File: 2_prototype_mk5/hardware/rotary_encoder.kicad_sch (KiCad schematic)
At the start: 2 parts, among them J8 Conn_01x05, SW2 PEC12R-2120F-S0012

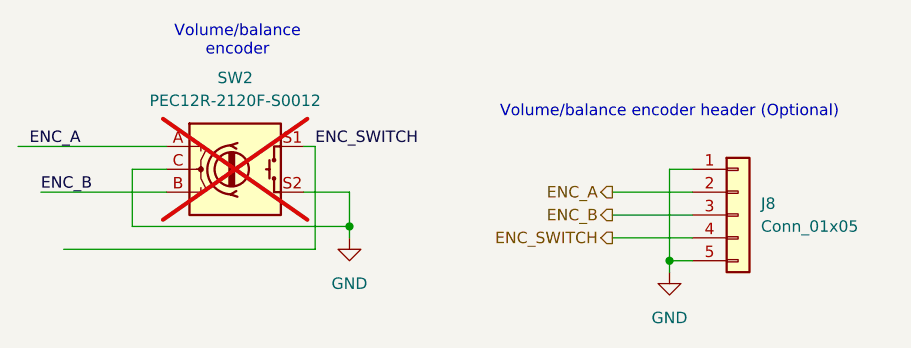
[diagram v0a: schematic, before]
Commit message: Major MKV redesign using embedded RP2350
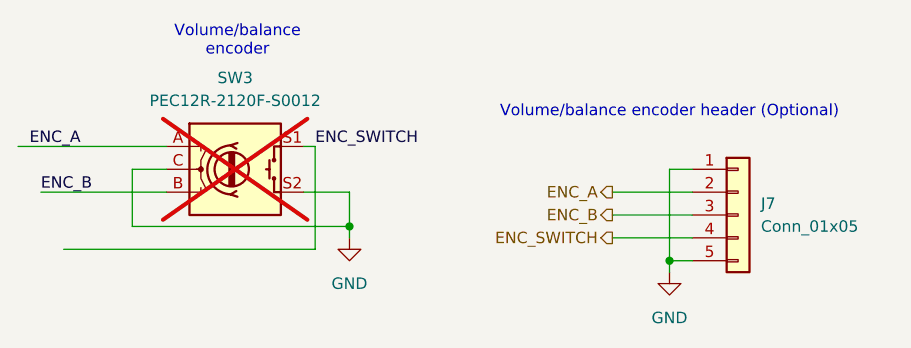
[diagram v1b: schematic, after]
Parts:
- renumbered J8 to J7, SW2 to SW3
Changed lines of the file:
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@@
 		(dnp no)
 		(fields_autoplaced yes)
-		(property "Reference" "#PWR031"
+		(property "Reference" "#PWR049"
 			(at 158.75 91.44 0)
 			(hide yes)
@@
 			(project "HDD Synth Prototype MK5"
 				(path "/1a22431a-ba36-40a0-9a7e-c2a82ec69c53/293c32c0-b0ed-4b60-a32a-d04548ae7be6"
-					(reference "#PWR031")
+					(reference "#PWR049")
 					(unit 1)
 				)
@@
 		(dnp yes)
 		(fields_autoplaced yes)
-		(property "Reference" "SW2"
+		(property "Reference" "SW3"
 			(at 146.05 67.31 0)
 			(show_name no)
@@
 			(project "HDD Synth Prototype MK5"
 				(path "/1a22431a-ba36-40a0-9a7e-c2a82ec69c53/293c32c0-b0ed-4b60-a32a-d04548ae7be6"
-					(reference "SW2")
+					(reference "SW3")
 					(unit 1)
 				)
@@
 		(dnp no)
 		(fields_autoplaced yes)
-		(property "Reference" "#PWR032"
+		(property "Reference" "#PWR050"
 			(at 194.31 95.25 0)
 			(hide yes)
@@
 			(project "HDD Synth Prototype MK5"
 				(path "/1a22431a-ba36-40a0-9a7e-c2a82ec69c53/293c32c0-b0ed-4b60-a32a-d04548ae7be6"
-					(reference "#PWR032")
+					(reference "#PWR050")
 					(unit 1)
 				)
@@
 		(dnp no)
 		(fields_autoplaced yes)
-		(property "Reference" "J8"
+		(property "Reference" "J7"
 			(at 204.47 81.2799 0)
 			(show_name no)
@@
 			(project "HDD Synth Prototype MK5"
 				(path "/1a22431a-ba36-40a0-9a7e-c2a82ec69c53/293c32c0-b0ed-4b60-a32a-d04548ae7be6"
-					(reference "J8")
+					(reference "J7")
 					(unit 1)
 				)

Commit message: MKV: Add LCSC numbers and resolve DRC errors
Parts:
- J7: LCSC_Part_Number (none) -> C124379
- SW3: LCSC_Part_Number PEC12R-2220F-S0024 -> (none)
